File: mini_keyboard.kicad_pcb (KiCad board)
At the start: 2 copper layers, 232.4 x 175.3 mm, 47 parts, among them J1 Conn_01x05_Male, SW1 SW_DIP_x01, SW10 SW_DIP_x01, SW11 SW_DIP_x01, SW12 SW_DIP_x01, SW13 SW_DIP_x01, SW14 SW_DIP_x01, SW15 SW_DIP_x01, SW16 SW_DIP_x01, SW17 SW_DIP_x01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

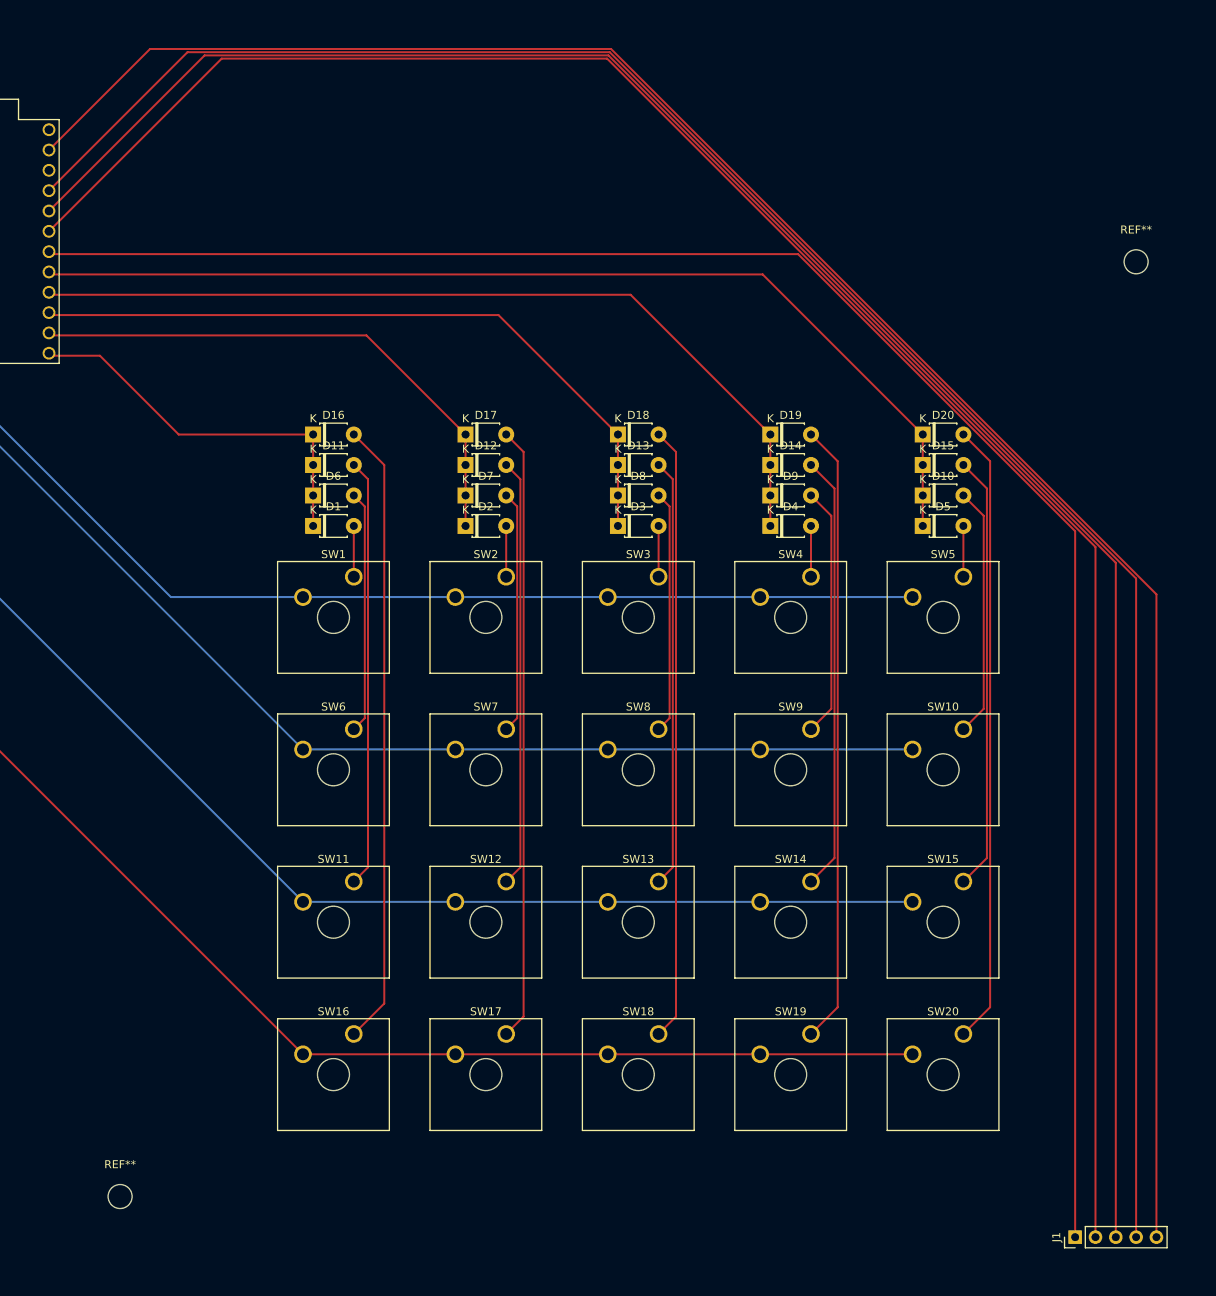
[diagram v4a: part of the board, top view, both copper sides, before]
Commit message: moved joystick up
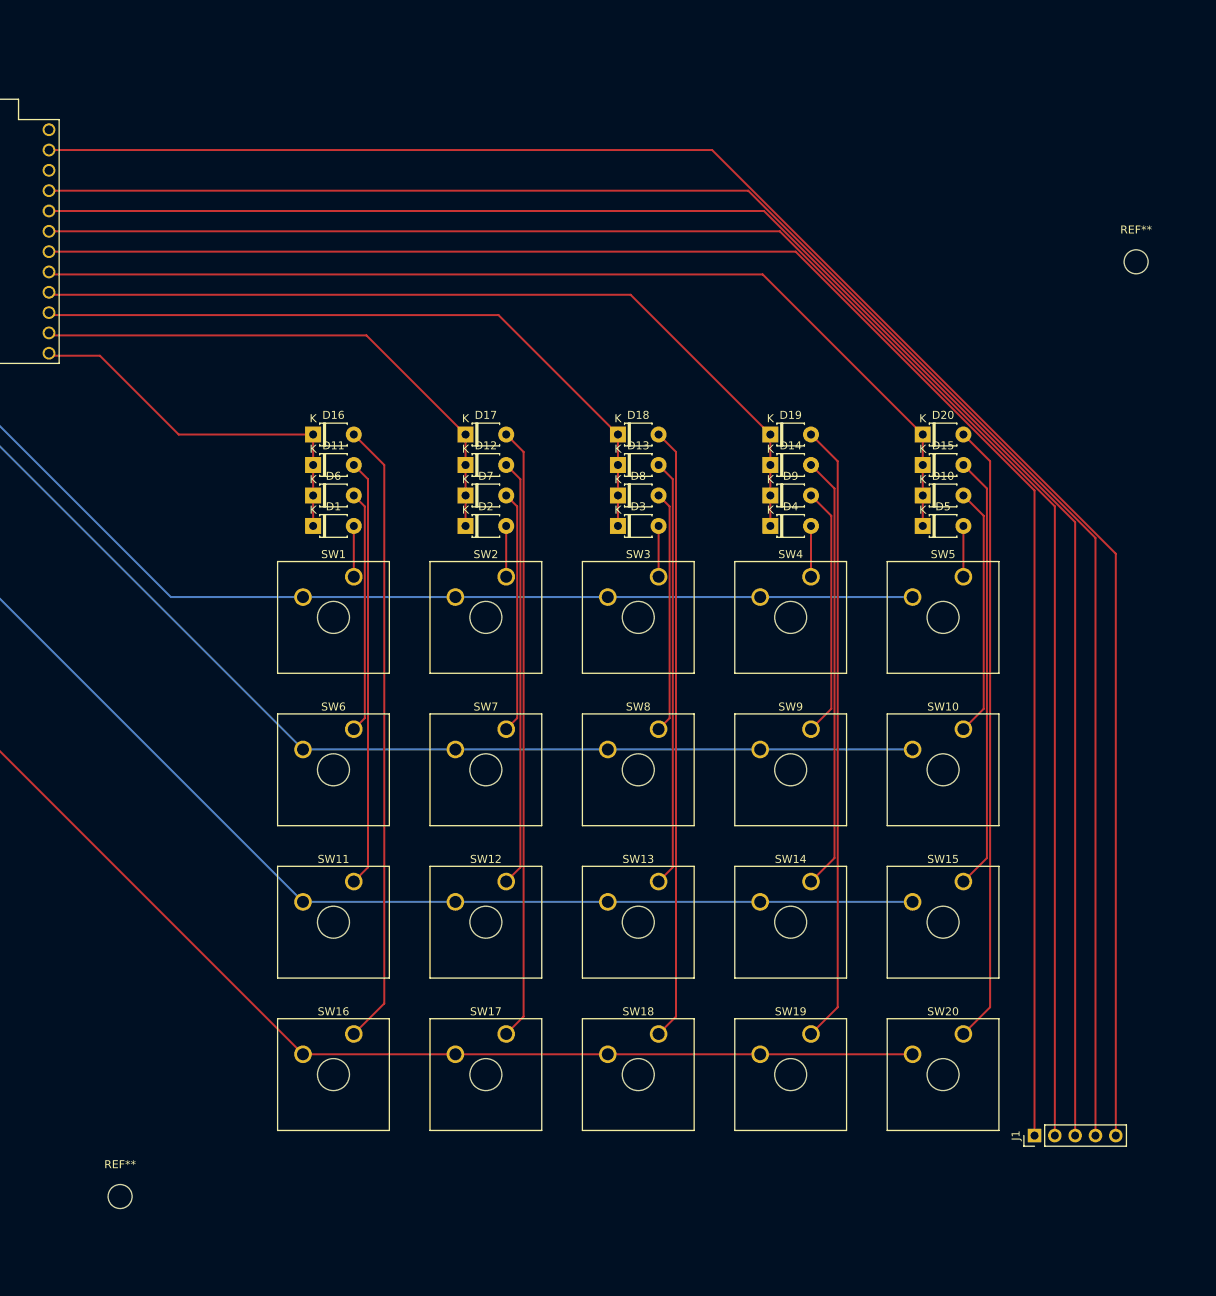
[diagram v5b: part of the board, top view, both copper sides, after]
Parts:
- moved J1 13.7 mm to (188.0, 129.5)
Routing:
- net Net-(J1-Pad2): track 251.3 -> 218.6 mm
- net Net-(J1-Pad3): track 252.0 -> 221.1 mm
- net Net-(J1-Pad4): track 252.6 -> 223.5 mm
- net Net-(J1-Pad5): track 252.2 -> 227.0 mm
- net Net-(J1-Pad1): track 231.0 -> 216.6 mm

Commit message: no cables
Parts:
- moved REF** 42.1 mm to (72.4, 34.3)
- moved U1 41.0 mm to (72.4, 55.9)
- moved REF** 16.5 mm to (207.0, 35.6)
- moved REF** 15.2 mm to (208.3, 135.9)
- moved SW11 10.2 mm to (98.1, 106.8)
- moved SW16 10.2 mm to (98.1, 125.8)
- moved SW6 10.2 mm to (98.1, 87.7)
- moved J1 9.16 mm to (188.0, 138.7)
- moved SW10 9.00 mm to (179.1, 87.7)
- moved SW12 9.00 mm to (121.9, 106.8)
- moved SW13 9.00 mm to (141.0, 106.8)
- moved SW14 9.00 mm to (160.0, 106.8)
- moved SW15 9.00 mm to (179.1, 106.8)
- moved SW17 9.00 mm to (121.9, 125.8)
- moved SW18 9.00 mm to (141.0, 125.8)
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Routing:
- net Net-(J1-Pad5): track 227.0 -> 0.00 mm
- net Net-(J1-Pad4): track 223.5 -> 0.00 mm
- net Net-(J1-Pad3): track 221.1 -> 0.00 mm
- net Net-(J1-Pad2): track 218.6 -> 0.00 mm
- net Net-(J1-Pad1): track 216.6 -> 0.00 mm
- net /out4: track 195.1 -> 0.00 mm
- net /out3: track 170.5 -> 0.00 mm
- net /out2: track 148.6 -> 0.00 mm
- net /out1: track 135.8 -> 0.00 mm
- net /in5: track 129.1 -> 0.00 mm
- net /in4: track 109.0 -> 0.00 mm
- net /in3: track 88.9 -> 0.00 mm
- net Net-(D16-Pad2): track 78.1 -> 0.00 mm
- net Net-(D20-Pad2): track 77.7 -> 0.00 mm
- net Net-(D19-Pad2): track 77.7 -> 0.00 mm
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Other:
- net class Default: trace_width 0.25 -> 0.4; via_dia 0.8 -> 1.2; via_drill 0.4 -> 0.6
- net class Power added: clearance 0.15, trace_width 1.27, via_dia 1.2, via_drill 0.6
- rule trace_min: 0.2 -> 0.4
- rule via_min_drill: 0.3 -> 0.6
- rule via_min_size: 0.4 -> 1.2

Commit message: Thick lines
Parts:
- moved REF** 10.5 mm to (62.2, 36.8)
- moved REF** 7.73 mm to (67.3, 134.6)
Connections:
- U1 pad 10: /out3 -> /out2
- U1 pad 11: /out2 -> /out3
- U1 pad 12: /out1 -> /out4
- U1 pad 9: /out4 -> /out1
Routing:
- net Net-(J1-Pad3): track 0.00 -> 214.8 mm
- net Net-(J1-Pad1): track 0.00 -> 214.6 mm
- net Net-(J1-Pad4): track 0.00 -> 214.6 mm
- net Net-(J1-Pad2): track 0.00 -> 214.6 mm
- net Net-(J1-Pad5): track 0.00 -> 212.5 mm
- net /out4: track 0.00 -> 150.7 mm
- net /in5: track 0.00 -> 121.0 mm
- net /in4: track 0.00 -> 103.6 mm
- net Net-(D20-Pad2): track 0.00 -> 86.5 mm
- net /in3: track 0.00 -> 86.1 mm
- net Net-(D18-Pad2): track 0.00 -> 86.0 mm
- net Net-(D17-Pad2): track 0.00 -> 86.0 mm
- net Net-(D16-Pad2): track 0.00 -> 86.0 mm
- net Net-(D19-Pad2): track 0.00 -> 86.0 mm
- net /in2: track 0.00 -> 68.7 mm
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
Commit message: Made out on right A_ ports
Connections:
- U1 pad 10: /out2 -> Net-(U1-Pad10)
- U1 pad 7: Net-(U1-Pad7) -> /out1
- U1 pad 9: /out1 -> /out2
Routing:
- net /out1: track 34.2 -> 36.3 mm
- net /out2: track 37.5 -> 39.2 mm
- net /out3: track 53.9 -> 53.2 mm
